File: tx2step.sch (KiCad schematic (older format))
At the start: 61 parts, among them CON1 BARREL_JACK, IC1 TPS2113A, IC2 ATMEGA328P-MM, IC3 MCP73831, IC4 TPS61202, IC5 DRV8834, IC6 DRV8834, J1 8P8C, J2 6P4C, J3 6P4C, J4 Debug, SW1 SW_DIP_x02, SW2 SW_DPDT_x2, SW3 SW_SPDT_MSM, Y1 16 MHz

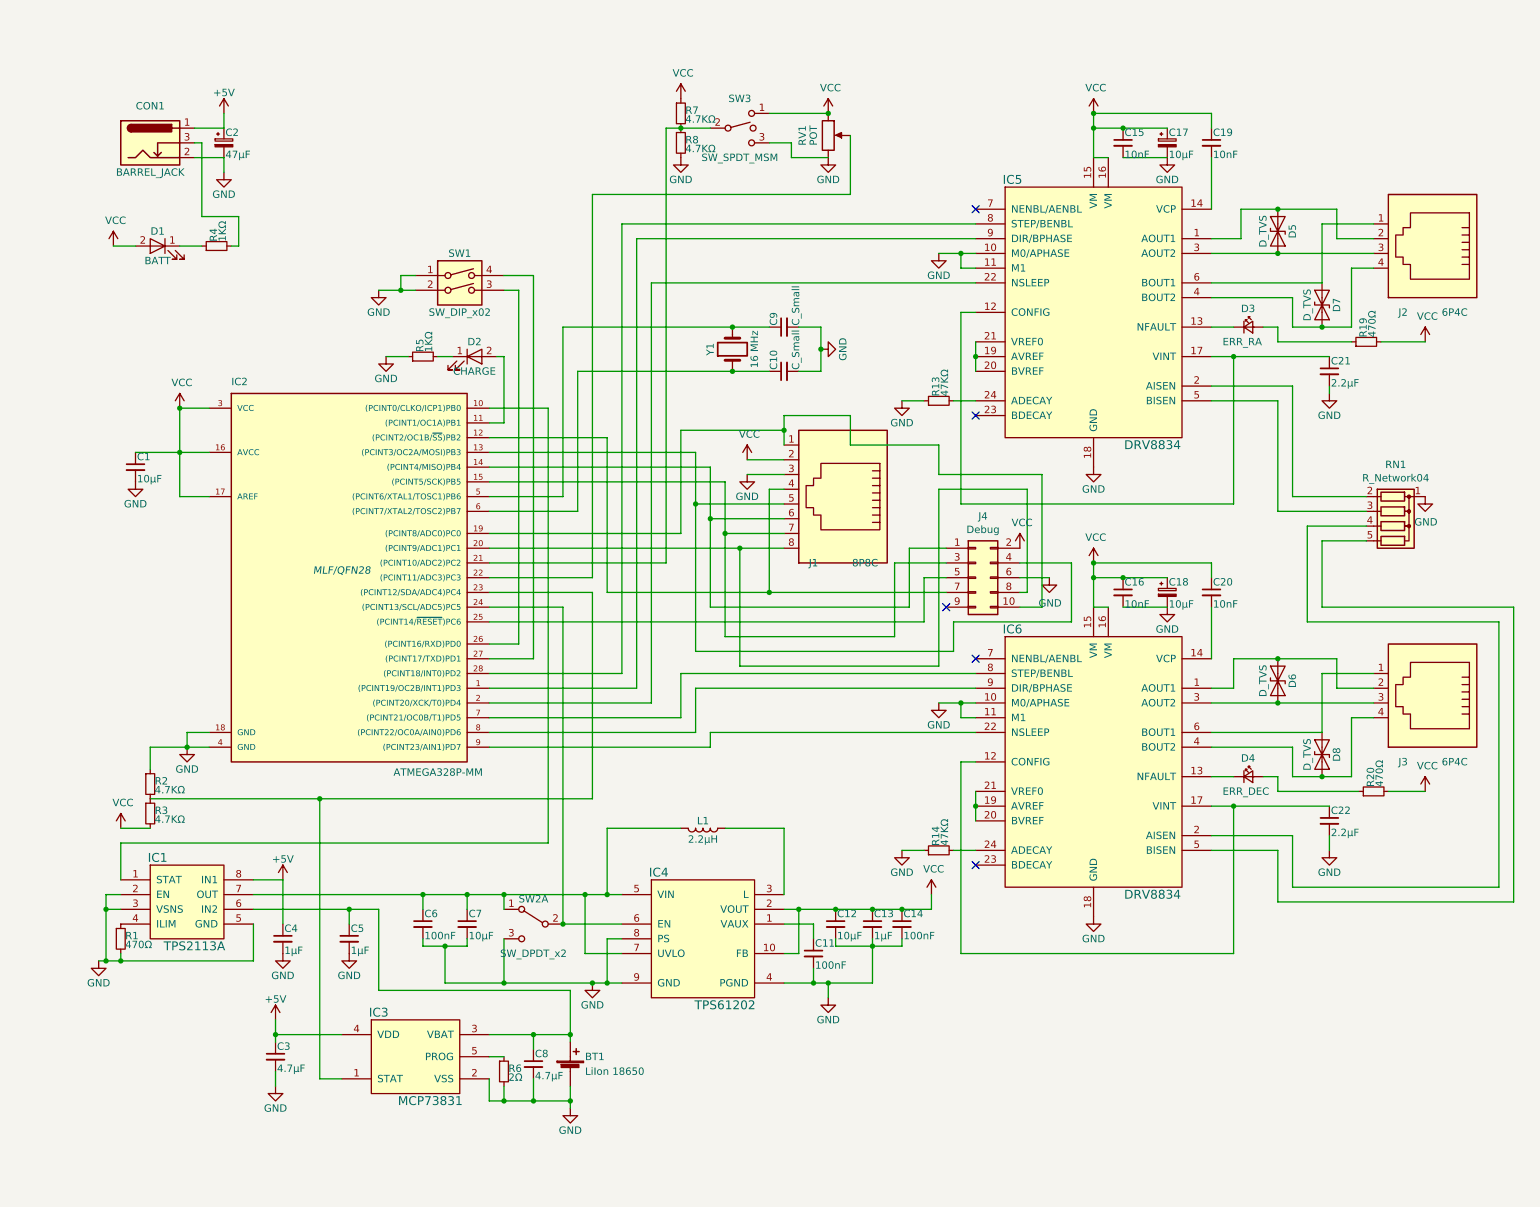
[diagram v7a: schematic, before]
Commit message: Use labeled nets
Clean up the schematic by using labeled nets between the ucontroller
and other components. Also remove the pin to the power switch, as
the microcontroller is no longer powered when the power switch is
off, and reuse it to detect whether the DC connector is plugged in.
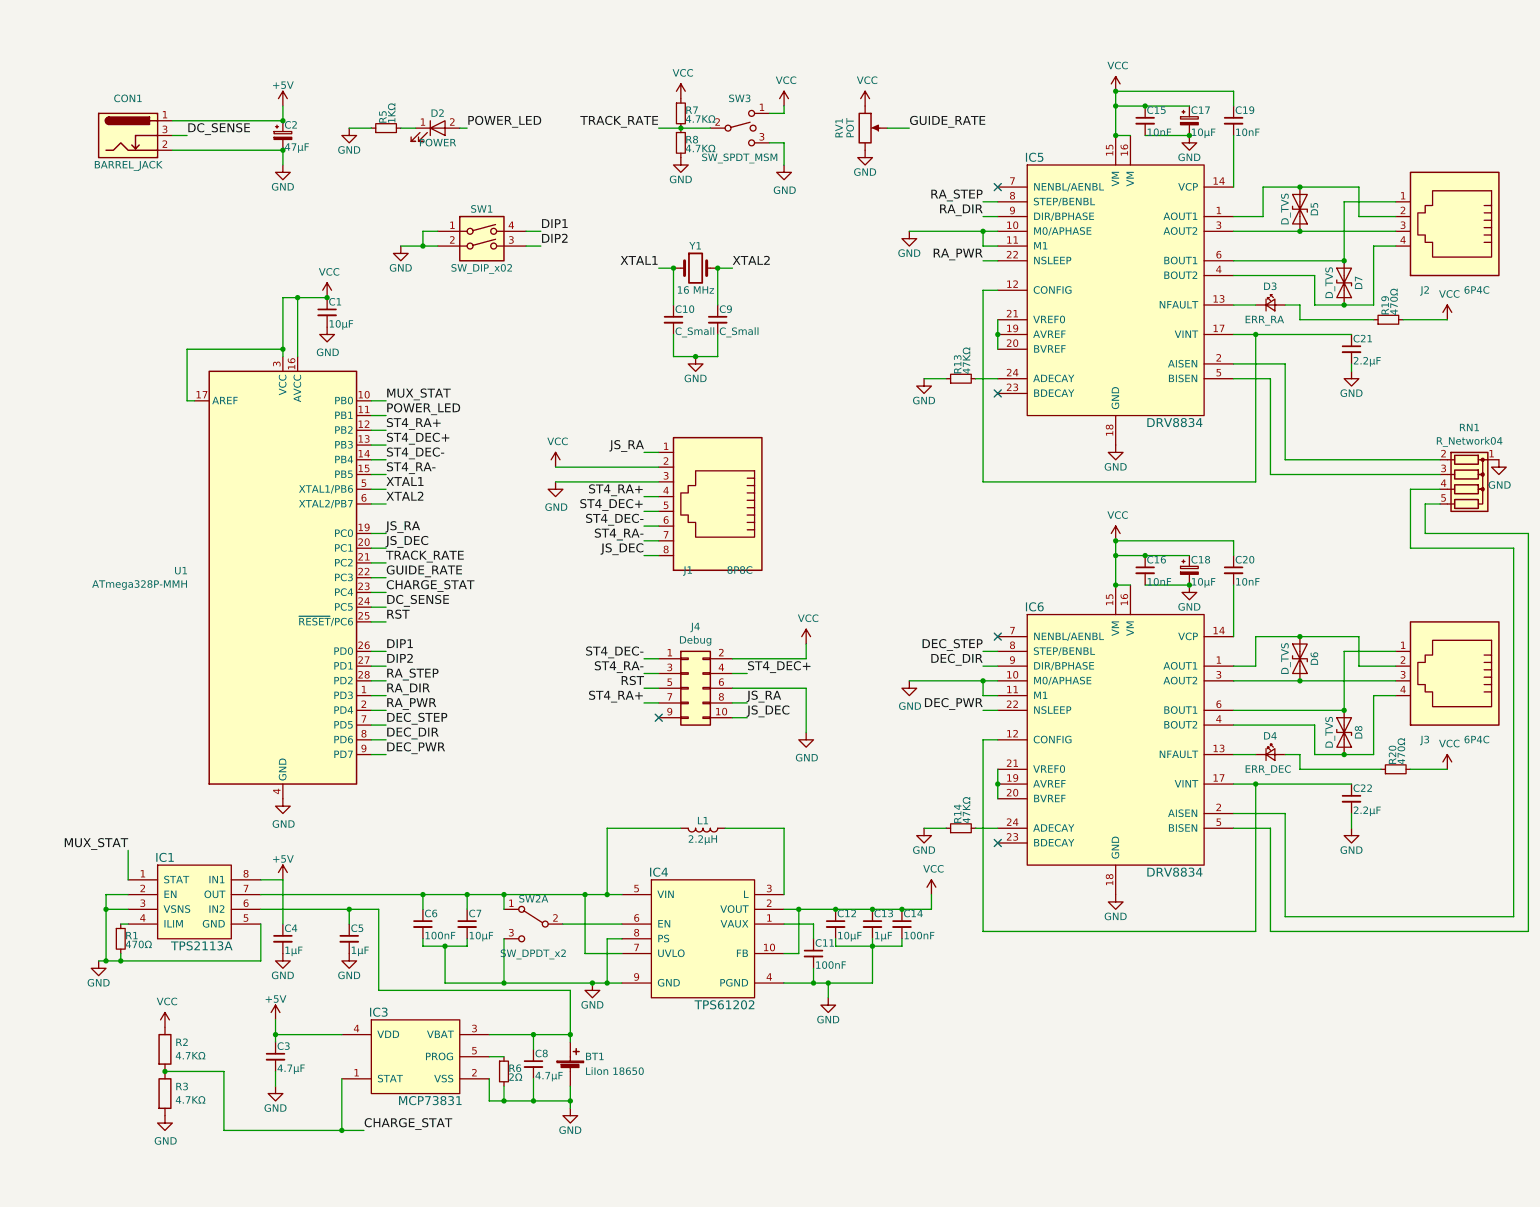
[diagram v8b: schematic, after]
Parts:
- removed D1: BATT, symbol tx2step-rescue:LED
- removed IC2: ATMEGA328P-MM, MLF/QFN28, symbol tx2step-rescue:ATMEGA328P-MM
- removed R2, R3: 4.7KΩ, symbol tx2step-rescue:R_Small
- removed R4: 1KΩ, symbol tx2step-rescue:R_Small
- added R2, R3: 4.7KΩ, symbol Device:R
- added U1: ATmega328P-MMH, Package_DFN_QFN:QFN-28-1EP_4x4mm_P0.45mm_EP2.4x2.4mm, symbol MCU_Microchip_ATmega:ATmega328P-MMH
- D2: value CHARGE -> POWER
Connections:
- net GND: now also R3.2, U1.18 (GND), U1.29 (GND), U1.4 (GND)
- net VCC: now also R2.1, U1.16 (AVCC), U1.17 (AREF), U1.3 (VCC)
- net RA_DIR: now reaches IC5.9 (DIR/BPHASE)
- net RA_DIR: now also U1.1 (PD3)
- net MUX_STAT: now reaches IC1.1 (STAT)
- net MUX_STAT: now also U1.10 (PB0)
- net POWER_LED: now reaches D2.2 (A)
- net POWER_LED: now also U1.11 (PB1)
- net ST4_RA+: now reaches J1.4, J4.7 (Pin_7)
- net ST4_RA+: now also U1.12 (PB2)
- net ST4_DEC+: now reaches J1.5, J4.4 (Pin_4)
- net ST4_DEC+: now also U1.13 (PB3)
- net ST4_DEC-: now reaches J1.6, J4.1 (Pin_1)
- net ST4_DEC-: now also U1.14 (PB4)
- net ST4_RA-: now reaches J1.7, J4.3 (Pin_3)
- net ST4_RA-: now also U1.15 (PB5)
- net JS_DEC: now reaches J4.10 (Pin_10)
- net JS_DEC: now also J1.8, U1.20 (PC1); no longer J1.1
- net RA_PWR: now reaches IC5.22 (NSLEEP)
- net RA_PWR: now also U1.2 (PD4)
- net JS_RA: now reaches J4.8 (Pin_8)
- net JS_RA: now also J1.1, U1.19 (PC0); no longer J1.8
- net TRACK_RATE: now reaches R7.2, R8.1, SW3.2
- net TRACK_RATE: now also U1.21 (PC2)
- net GUIDE_RATE: now reaches RV1.2
- net GUIDE_RATE: now also U1.22 (PC3)
- net CHARGE_STAT: now reaches IC3.1 (STAT)
- net CHARGE_STAT: now also R2.2, R3.1, U1.23 (PC4)
- net RST: now reaches J4.5 (Pin_5)
- net RST: now also U1.25 (~RESET~/PC6)
- net DIP2: now reaches SW1.3
- net DIP2: now also U1.27 (PD1)
- net DIP1: now reaches SW1.4
- net DIP1: now also U1.26 (PD0)
- net RA_STEP: now reaches IC5.8 (STEP/BENBL)
- net RA_STEP: now also U1.28 (PD2)
- net XTAL2: now reaches C9.1, Y1.2
- net XTAL2: now also U1.6 (XTAL2/PB7)
- net XTAL1: now reaches C10.1, Y1.1
- net XTAL1: now also U1.5 (XTAL1/PB6)
- net DEC_STEP: now reaches IC6.8 (STEP/BENBL)
- net DEC_STEP: now also U1.7 (PD5)
- net DEC_DIR: now reaches IC6.9 (DIR/BPHASE)
- net DEC_DIR: now also U1.8 (PD6)
- net DEC_PWR: now reaches IC6.22 (NSLEEP)
- net DEC_PWR: now also U1.9 (PD7)
- net DC_SENSE: now reaches CON1.3
- net DC_SENSE: now also U1.24 (PC5)
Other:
- moved on the sheet: C1, C10, C15, C16, C17, C18, C19, C2, C20, C21, C22, C9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
